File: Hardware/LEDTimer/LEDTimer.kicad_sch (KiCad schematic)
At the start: 25 parts, among them J1 ICSP, J2 LED, J3 PWR_IN, SW1 SW_Push, SW2 SW_Push, SW3 SW_Push, U1 AP7383-36WW7, U2 PIC16F1825, U3 Display_128x64_096_I2C, U4 BCR_421U_E6327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

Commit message: Update the resistor values of the LDO_SENSE divider
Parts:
- R1: value 24k -> 47k
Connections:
- net VBAT_SENSE: no longer names the net of BT1.1 (+), D1.1
- net VBAT_SENSE: no longer U2.8 (RC2)
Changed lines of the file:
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@@
   (junction (at 111.76 128.27) (diameter 0) (color 0 0 0 0)
   )
-  (junction (at 76.2 39.37) (diameter 0) (color 0 0 0 0)
-  )
   (junction (at 53.34 52.07) (diameter 0) (color 0 0 0 0)
   )
@@
     (stroke (width 0) (type default) (color 0 0 0 0))
   )
-  (wire (pts (xy 172.72 106.68) (xy 188.595 106.68))
-    (stroke (width 0) (type default) (color 0 0 0 0))
-  )
   (wire (pts (xy 124.46 128.27) (xy 124.46 130.81))
     (stroke (width 0) (type default) (color 0 0 0 0))
@@
     (stroke (width 0) (type default) (color 0 0 0 0))
   )
-  (wire (pts (xy 76.2 39.37) (xy 81.28 39.37))
-    (stroke (width 0) (type default) (color 0 0 0 0))
-  )
   (wire (pts (xy 26.67 41.91) (xy 26.67 52.07))
     (stroke (width 0) (type default) (color 0 0 0 0))
@@
   (wire (pts (xy 198.12 66.675) (xy 198.12 67.945))
     (stroke (width 0) (type default) (color 0 0 0 0))
-  )
-  (label "VBAT_SENSE" (at 188.595 106.68 180)
-    (effects (font (size 1.27 1.27)) (justify right bottom))
   )
   (label "~{MCLR}{slash}VPP" (at 140.335 99.06 180)
     (effects (font (size 1.27 1.27)) (justify right bottom))
-  )
-  (label "VBAT_SENSE" (at 81.28 39.37 0)
-    (effects (font (size 1.27 1.27)) (justify left bottom))
   )
   (label "~{MCLR}{slash}VPP" (at 148.59 33.655 0)
@@
       (effects (font (size 1.27 1.27)) (justify left))
     )
-    (property "Value" "24k" (id 1) (at 99.06 34.2899 0)
+    (property "Value" "47k" (id 1) (at 99.06 34.2899 0)
       (effects (font (size 1.27 1.27)) (justify left))
     )
@@
     )
     (path "/c5745adf-2a60-4943-991a-b58822c9fa8c"
-      (reference "R1") (unit 1) (value "24k") (footprint "Resistor_SMD:R_0805_2012Metric_Pad1.20x1.40mm_HandSolder")
+      (reference "R1") (unit 1) (value "47k") (footprint "Resistor_SMD:R_0805_2012Metric_Pad1.20x1.40mm_HandSolder")
     )
     (path "/b2d760ee-df69-47a2-870c-d81d69e6c770"

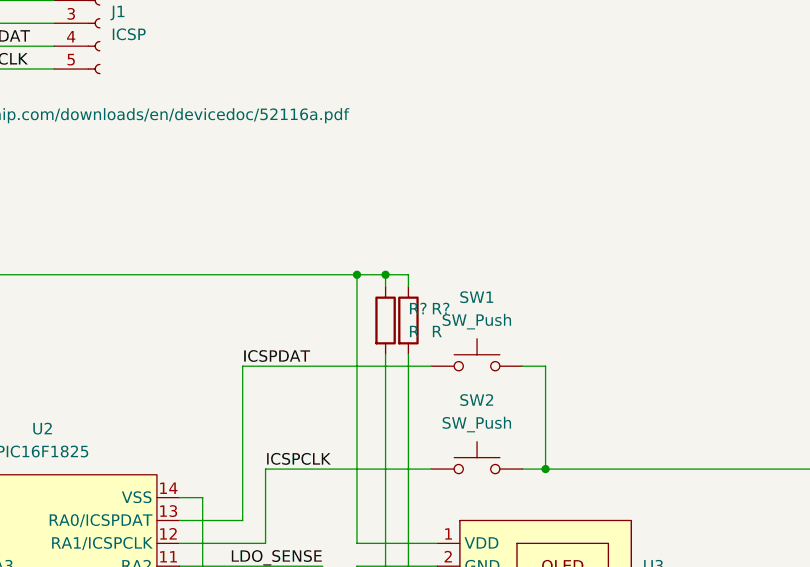
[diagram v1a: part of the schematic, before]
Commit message: Add missing values to I2C pull-up resistors
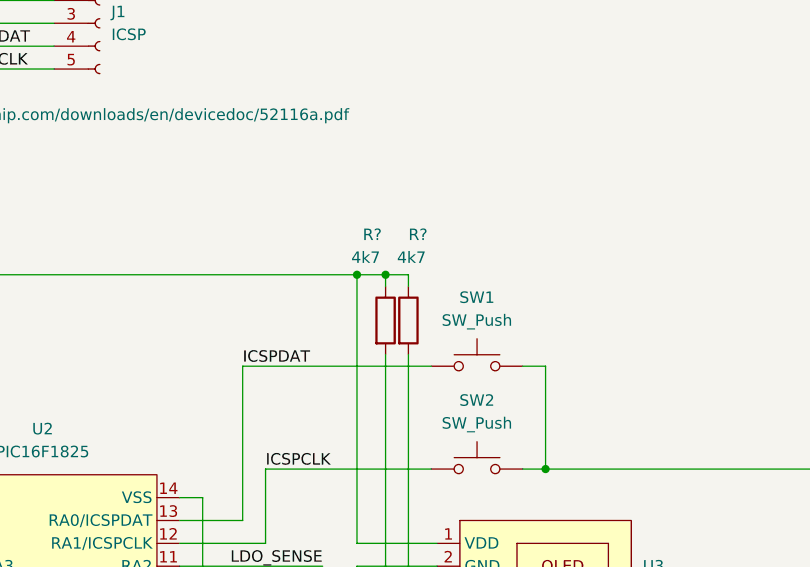
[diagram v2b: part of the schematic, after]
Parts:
- R? (x2): value R -> 4k7
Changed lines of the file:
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@@
   )
   (symbol (lib_id "Device:R") (at 195.58 71.755 0) (unit 1)
-    (in_bom yes) (on_board yes) (fields_autoplaced)
-    (property "Reference" "R?" (id 0) (at 198.12 70.4849 0)
-      (effects (font (size 1.27 1.27)) (justify left))
-    )
-    (property "Value" "R" (id 1) (at 198.12 73.0249 0)
+    (in_bom yes) (on_board yes)
+    (property "Reference" "R?" (id 0) (at 193.04 62.23 0)
+      (effects (font (size 1.27 1.27)) (justify left))
+    )
+    (property "Value" "4k7" (id 1) (at 191.77 64.77 0)
       (effects (font (size 1.27 1.27)) (justify left))
     )
@@
   )
   (symbol (lib_id "Device:R") (at 198.12 71.755 0) (unit 1)
-    (in_bom yes) (on_board yes) (fields_autoplaced)
-    (property "Reference" "R?" (id 0) (at 200.66 70.4849 0)
-      (effects (font (size 1.27 1.27)) (justify left))
-    )
-    (property "Value" "R" (id 1) (at 200.66 73.0249 0)
+    (in_bom yes) (on_board yes)
+    (property "Reference" "R?" (id 0) (at 198.12 62.23 0)
+      (effects (font (size 1.27 1.27)) (justify left))
+    )
+    (property "Value" "4k7" (id 1) (at 196.85 64.77 0)
       (effects (font (size 1.27 1.27)) (justify left))
     )
@@
     )
     (path "/7e6fc124-3231-4c18-b624-42f84a9548d8"
-      (reference "R?") (unit 1) (value "R") (footprint "")
+      (reference "R?") (unit 1) (value "4k7") (footprint "")
     )
     (path "/94034e64-17d7-4c11-8df7-c281c016c2b8"
-      (reference "R?") (unit 1) (value "R") (footprint "")
+      (reference "R?") (unit 1) (value "4k7") (footprint "")
     )
     (path "/e4af397d-0487-4cbc-84e3-6d89c4326703"

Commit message: PCB: add footprint libraries
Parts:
- removed BT1: CR2032, symbol Device:Battery_Cell
- removed Rext1: R, Resistor_SMD:R_0805_2012Metric_Pad1.20x1.40mm_HandSolder, symbol Device:R
- removed Y1: 32.768kHz, Crystal:Crystal_AT310_D3.0mm_L10.0mm_Horizontal_1EP_style2, symbol Device:Crystal
- added BT1: HU2032-LF, Renata HU2032LF:Renata-HU2032-LF-0-0-0, symbol Renata HU2032LF:HU2032-LF
- added RVext1: R_Potentiometer, Potentiometer_SMD:Potentiometer_Vishay_TS53YJ_Vertical, symbol Device:R_Potentiometer
- added SW4: SW_SPDT, SPDT Switch:1825232-1, symbol Switch:SW_SPDT
- added Y1: 32.768 kHz, Crystal:Crystal_SMD_Abracon_ABS25-4Pin_8.0x3.8mm, symbol Device:Crystal_GND23
- R4, R6: renamed from R?; footprint (none) -> Resistor_SMD:R_0805_2012Metric_Pad1.20x1.40mm_HandSolder
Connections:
- net GND: now also BT1.1 (CATHODE), RVext1.3, Y1.2, Y1.3
- net at D1.1: now also SW4.1 (A)
- net at CG1.1, U2.2 (RA5): now also Y1.1
- net at CD1.1, RD1.2: now also Y1.4
- net at U4.6 (Rext): now also RVext1.1, RVext1.2
- new net: BT1.2 (ANODE), SW4.2 (B)
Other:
- company: (none) -> github.com/tomikaa87
- title: (none) -> LED Timer

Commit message: PCB: start laying out the board
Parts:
- removed R5: 1k, Resistor_SMD:R_0805_2012Metric_Pad1.20x1.40mm_HandSolder, symbol Device:R
- SW1, SW2, SW3: footprint Button_Switch_SMD:SW_Push_1P1T_NO_6x6mm_H9.5mm -> LEDTimer:EVQ9P701P
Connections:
- net GND: now also SW1.1, SW2.1; no longer SW1.2, SW2.2
- net ICSPCLK: now also SW2.2; no longer SW2.1
- net ICSPDAT: now also SW1.2; no longer SW1.1
- net LED_EN_PWM: now also U4.1 (EN)
- net at C2.1, R1.1, U1.5 (VOUT): now also D1.1; no longer D1.2
- net at BT1.2 (ANODE): now also SW4.1 (A); no longer SW4.2 (B)
- new net: D1.2, SW4.2 (B)
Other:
- moved on the sheet: BT1, D1, SW4

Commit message: PCB: first version of the layout
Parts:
- D1: footprint Package_TO_SOT_SMD:SOT-23 -> Package_TO_SOT_SMD:SOT-416
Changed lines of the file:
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@@
     (property "Reference" "D1" (id 0) (at 66.04 43.18 0))
     (property "Value" "BAT54C" (id 1) (at 66.04 45.72 0))
-    (property "Footprint" "Package_TO_SOT_SMD:SOT-23" (id 2) (at 67.945 42.545 0)
+    (property "Footprint" "Package_TO_SOT_SMD:SOT-416" (id 2) (at 67.945 42.545 0)
       (effects (font (size 1.27 1.27)) (justify left) hide)
     )
@@
     )
     (path "/fff8192d-12e8-4d67-ae96-488e592bbcc2"
-      (reference "D1") (unit 1) (value "BAT54C") (footprint "Package_TO_SOT_SMD:SOT-23")
+      (reference "D1") (unit 1) (value "BAT54C") (footprint "Package_TO_SOT_SMD:SOT-416")
     )
     (path "/a074c02e-cb09-4f77-8b38-7831a3988ff3"

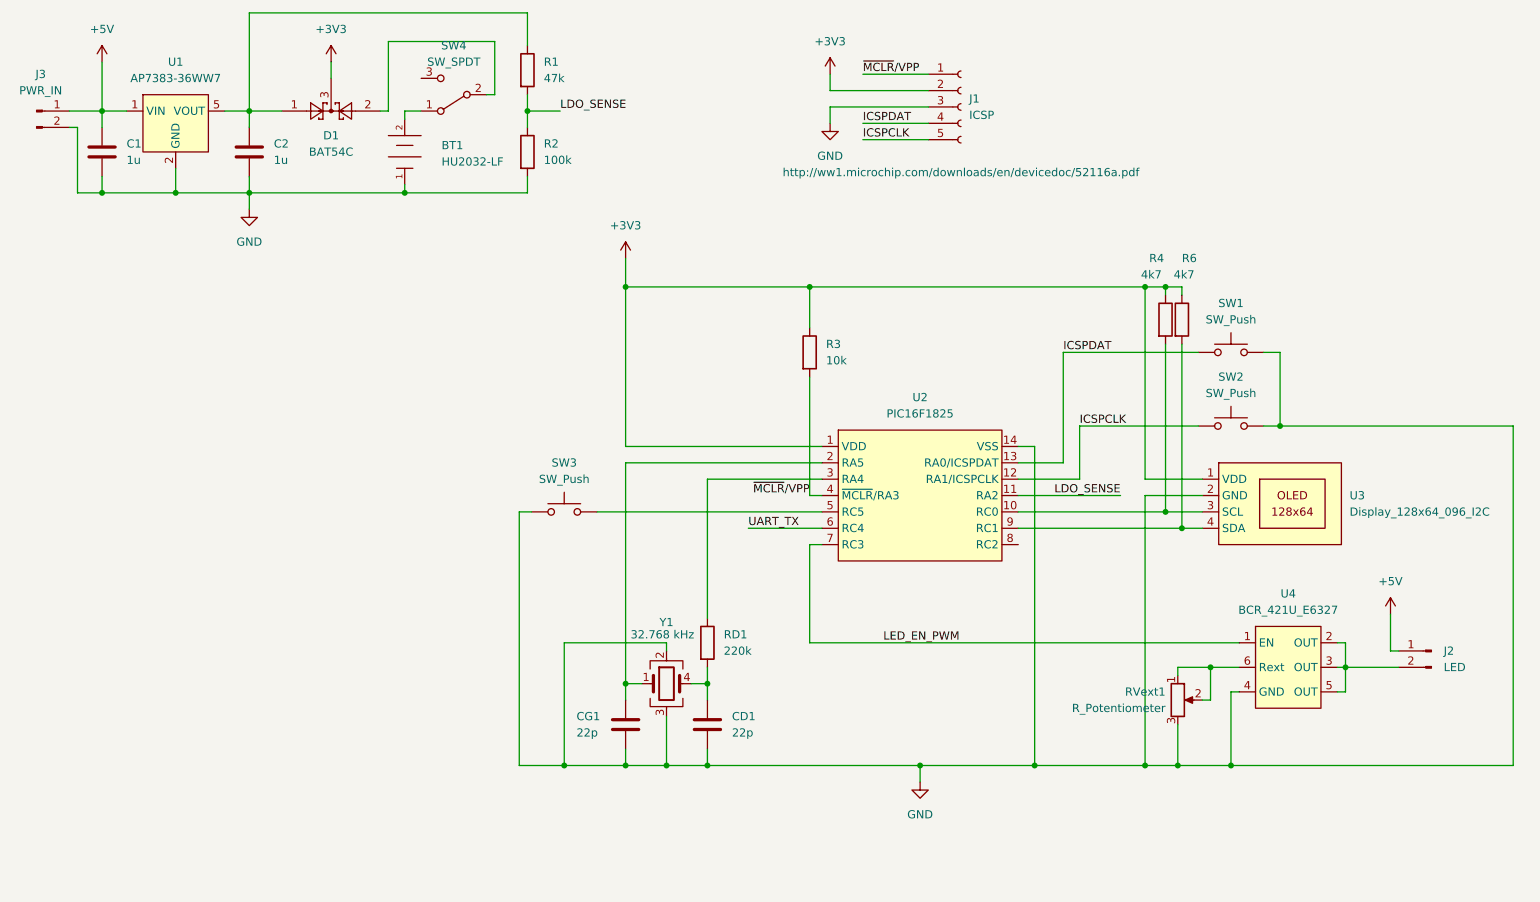
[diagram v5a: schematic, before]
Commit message: PCB: new layout (not routed yet)
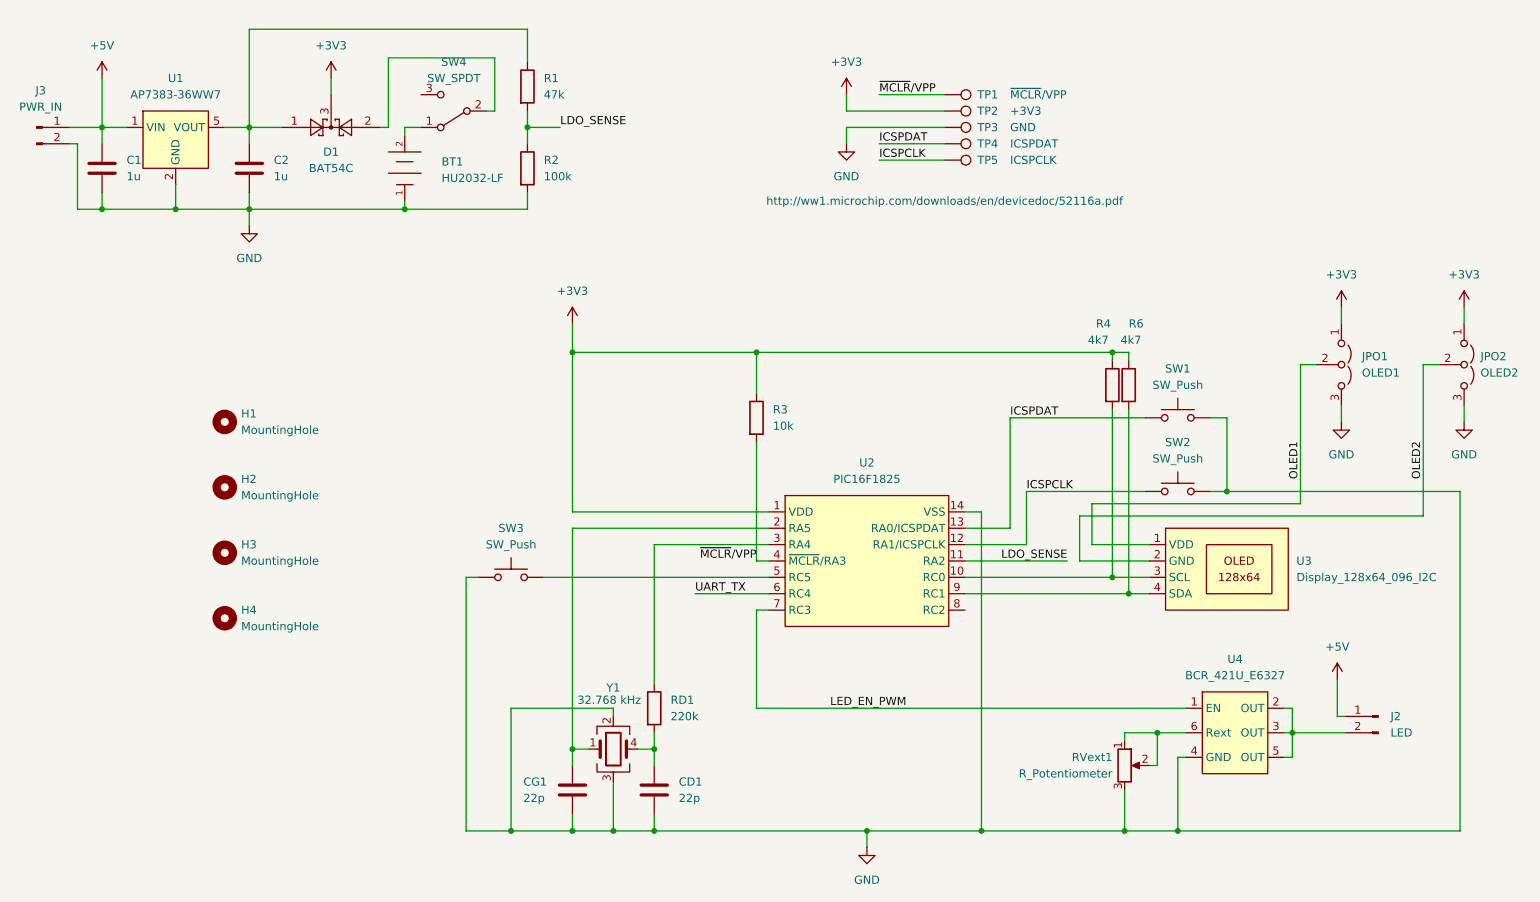
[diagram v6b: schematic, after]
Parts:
- removed J1: ICSP, Connector_PinHeader_2.54mm:PinHeader_1x05_P2.54mm_Vertical, symbol Connector:Conn_01x05_Female
- added H1, H2, H3, H4: MountingHole, MountingHole:MountingHole_2.2mm_M2, symbol Mechanical:MountingHole
- added JPO1: OLED1, Jumper:SolderJumper-3_P1.3mm_Open_RoundedPad1.0x1.5mm, symbol Jumper:Jumper_3_Open
- added JPO2: OLED2, Jumper:SolderJumper-3_P1.3mm_Open_RoundedPad1.0x1.5mm, symbol Jumper:Jumper_3_Open
- added TP1: ~{MCLR}/VPP, TestPoint:TestPoint_Pad_D1.5mm, symbol Connector:TestPoint
- added TP2: +3V3, TestPoint:TestPoint_Pad_D1.5mm, symbol Connector:TestPoint
- added TP3: GND, TestPoint:TestPoint_Pad_D1.5mm, symbol Connector:TestPoint
- added TP4: ICSPDAT, TestPoint:TestPoint_Pad_D1.5mm, symbol Connector:TestPoint
- added TP5: ICSPCLK, TestPoint:TestPoint_Pad_D1.5mm, symbol Connector:TestPoint
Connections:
- net +3V3: now also JPO1.1 (A), JPO2.1 (A), TP2.1; no longer U3.1 (VDD)
- net GND: now also JPO1.3 (B), JPO2.3 (B), TP3.1; no longer U3.2 (GND)
- net ICSPCLK: now also TP5.1
- net ICSPDAT: now also TP4.1
- net ~{MCLR}/VPP: now also TP1.1
- new net OLED1: JPO1.2 (C), U3.1 (VDD)
- new net OLED2: JPO2.2 (C), U3.2 (GND)
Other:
- moved on the sheet: BT1, C1, C2, CD1, CG1, D1, J2, J3, R1, R2, R3, R4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

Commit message: PCB: use a 4-layer design
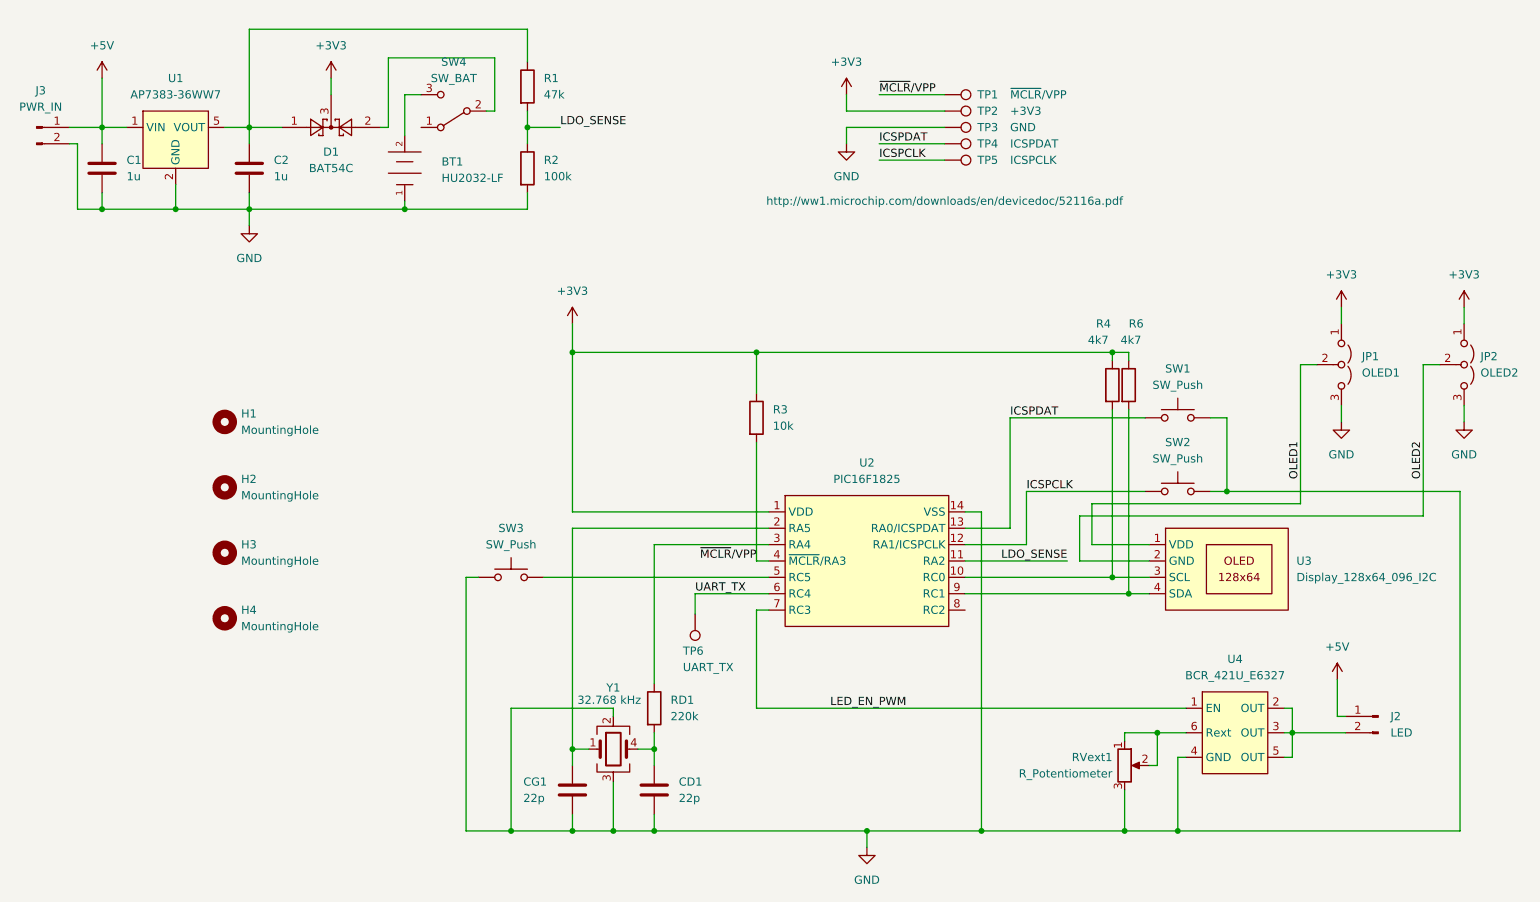
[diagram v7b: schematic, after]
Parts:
- added TP6: UART_TX, TestPoint:TestPoint_Pad_D1.5mm, symbol Connector:TestPoint
- SW4: value SW_SPDT -> SW_BAT
- renumbered JPO1 to JP1, JPO2 to JP2
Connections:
- net UART_TX: now also TP6.1
- net at BT1.2 (ANODE): now also SW4.3 (C); no longer SW4.1 (A)
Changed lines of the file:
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@@
+    (stroke (width 0) (type default) (color 0 0 0 0))
+  )
+  (wire (pts (xy 80.01 36.83) (xy 77.47 36.83))
     (stroke (width 0) (type default) (color 0 0 0 0))
   )
@@
     (stroke (width 0) (type default) (color 0 0 0 0))
   )
-  (wire (pts (xy 77.47 41.91) (xy 77.47 43.18))
+  (wire (pts (xy 77.47 36.83) (xy 77.47 43.18))
     (stroke (width 0) (type default) (color 0 0 0 0))
   )
@@
     (stroke (width 0) (type default) (color 0 0 0 0))
   )
-  (wire (pts (xy 80.01 41.91) (xy 77.47 41.91))
-    (stroke (width 0) (type default) (color 0 0 0 0))
-  )
   (wire (pts (xy 53.34 54.61) (xy 77.47 54.61))
     (stroke (width 0) (type default) (color 0 0 0 0))
@@
   )
   (wire (pts (xy 164.465 111.76) (xy 187.325 111.76))
+    (stroke (width 0) (type default) (color 0 0 0 0))
+  )
+  (wire (pts (xy 122.555 114.3) (xy 122.555 117.475))
     (stroke (width 0) (type default) (color 0 0 0 0))
   )
@@
   (symbol (lib_id "Jumper:Jumper_3_Open") (at 241.935 78.74 270) (unit 1)
     (in_bom yes) (on_board yes) (fields_autoplaced)
-    (property "Reference" "JPO2" (id 0) (at 244.475 77.4699 90)
+    (property "Reference" "JP2" (id 0) (at 244.475 77.4699 90)
       (effects (font (size 1.27 1.27)) (justify left))
     )
@@
   (symbol (lib_id "Jumper:Jumper_3_Open") (at 222.885 78.74 270) (unit 1)
     (in_bom yes) (on_board yes) (fields_autoplaced)
-    (property "Reference" "JPO1" (id 0) (at 226.06 77.4699 90)
+    (property "Reference" "JP1" (id 0) (at 226.06 77.4699 90)
       (effects (font (size 1.27 1.27)) (justify left))
     )
@@
     (pin "2")
     (pin "3")
+  )
+  (symbol (lib_id "Connector:TestPoint") (at 122.555 117.475 180) (unit 1)
+    (in_bom yes) (on_board yes)
+    (property "Reference" "TP6" (id 0) (at 120.65 123.19 0)
+      (effects (font (size 1.27 1.27)) (justify right))
+    )
+    (property "Value" "UART_TX" (id 1) (at 120.65 125.73 0)
+      (effects (font (size 1.27 1.27)) (justify right))
+    )
+    (property "Footprint" "TestPoint:TestPoint_Pad_D1.5mm" (id 2) (at 117.475 117.475 0)
+      (effects (font (size 1.27 1.27)) hide)
+    )
+    (property "Datasheet" "~" (id 3) (at 117.475 117.475 0)
+      (effects (font (size 1.27 1.27)) hide)
+    )
+    (pin "1")
   )
   (symbol (lib_id "power:+3V3") (at 66.04 34.29 0) (unit 1)
@@
       (effects (font (size 1.27 1.27)) (justify left))
     )
-    (property "Value" "~{MCLR}/VPP" (id 1) (at 171.45 36.8301 90)
+    (property "Value" "~{MCLR}/VPP" (id 1) (at 171.45 36.83 90)
       (effects (font (size 1.27 1.27)) (justify left))
     )
@@
     (in_bom yes) (on_board yes) (fields_autoplaced)
     (property "Reference" "SW4" (id 0) (at 85.09 31.75 0))
-    (property "Value" "SW_SPDT" (id 1) (at 85.09 34.29 0))
+    (property "Value" "SW_BAT" (id 1) (at 85.09 34.29 0))
     (property "Footprint" "SPDT Switch:1825232-1" (id 2) (at 85.09 39.37 0)
       (effects (font (size 1.27 1.27)) hide)
@@
     )
     (path "/ca50989c-806e-4138-b3ff-f2b2f96652a0"
-      (reference "JPO1") (unit 1) (value "OLED1") (footprint "Jumper:SolderJumper-3_P1.3mm_Open_RoundedPad1.0x1.5mm")
+      (reference "JP1") (unit 1) (value "OLED1") (footprint "Jumper:SolderJumper-3_P1.3mm_Open_RoundedPad1.0x1.5mm")
     )
     (path "/3f772120-8435-4569-9ddb-0201d4f94057"
-      (reference "JPO2") (unit 1) (value "OLED2") (footprint "Jumper:SolderJumper-3_P1.3mm_Open_RoundedPad1.0x1.5mm")
+      (reference "JP2") (unit 1) (value "OLED2") (footprint "Jumper:SolderJumper-3_P1.3mm_Open_RoundedPad1.0x1.5mm")
     )
     (path "/c5745adf-2a60-4943-991a-b58822c9fa8c"
@@
     )
     (path "/e49a9939-e5f7-4dfe-8005-f25d0240725f"
-      (reference "SW4") (unit 1) (value "SW_SPDT") (footprint "SPDT Switch:1825232-1")
+      (reference "SW4") (unit 1) (value "SW_BAT") (footprint "SPDT Switch:1825232-1")
     )
     (path "/da811b11-3f5c-4085-9312-63fa595b7c79"
@@
       (reference "TP5") (unit 1) (value "ICSPCLK") (footprint "TestPoint:TestPoint_Pad_D1.5mm")
     )
+    (path "/ce0a664b-9c29-44eb-9522-6b329ca1e2bc"
+      (reference "TP6") (unit 1) (value "UART_TX") (footprint "TestPoint:TestPoint_Pad_D1.5mm")
+    )
     (path "/8788c6d3-a91d-4a59-bb7e-ca7937ac1770"
